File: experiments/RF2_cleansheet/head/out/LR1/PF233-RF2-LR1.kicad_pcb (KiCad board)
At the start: 2 copper layers, 150 x 150 mm, 94 parts

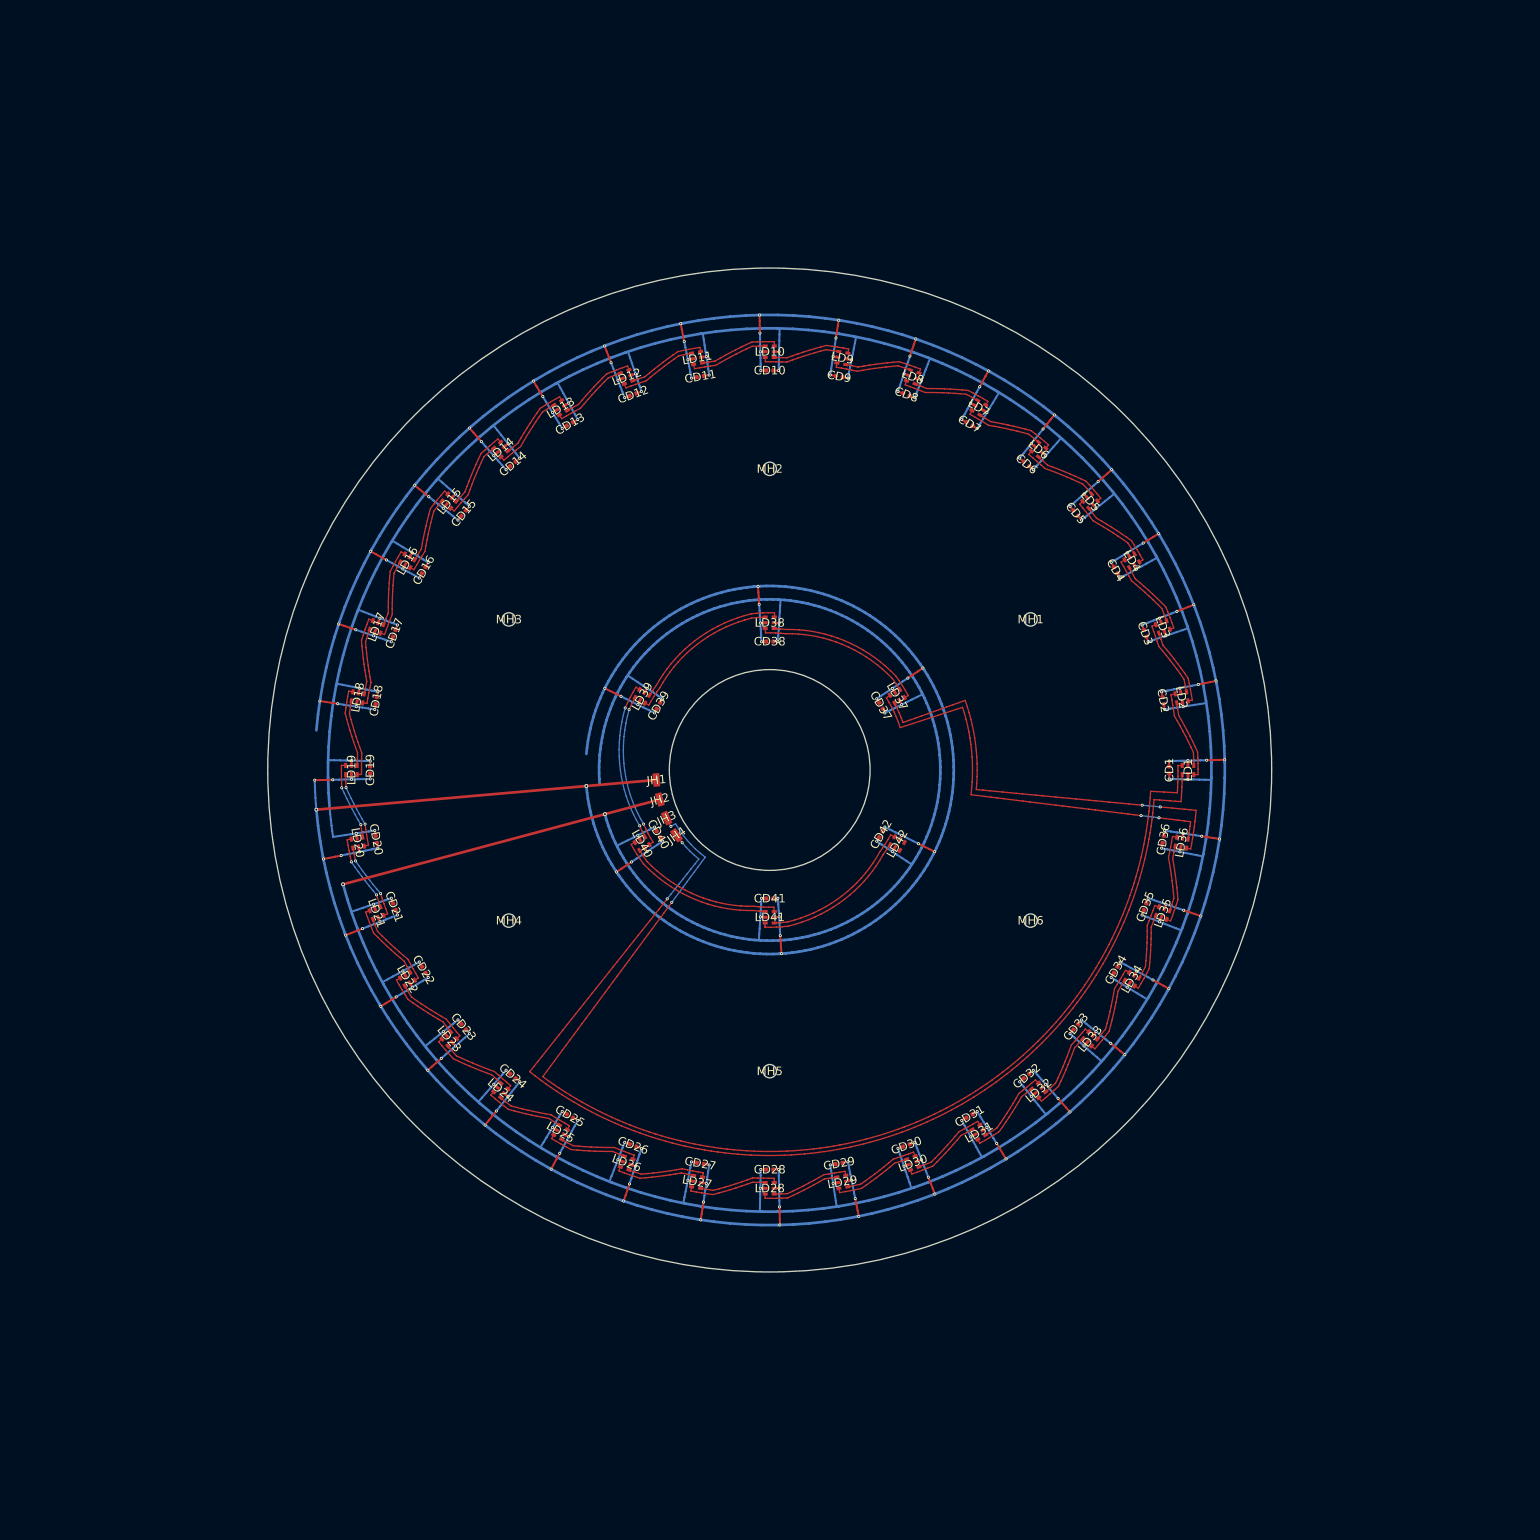
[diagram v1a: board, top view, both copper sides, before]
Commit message: RF2 WIP: dense LED display flex LR1 (522 SK9822-EC20, 13 rings rim to centre), template-routed, KiCad DRC 0 / 0 unconnected
rf2_ledgrid.py is the single source of the display's outline, parts, nets and copper: 12 rings r 104..16 on an 8 mm grid + a 4-LED centre ring,
alternating CCW / CW cells sharing open B.Cu buses, two B.Cu spokes (power tree), 4 serpentine chains (48 / 101 / 158 / 215 LEDs), hinge flap
above CB1D with 12 lands, notch around the gland boss, 6 rim holes. Min clearance 0.15 mm (rule 0.10), no loop around the axis, parity, Gerbers.
Housing, power budget and docs follow.

Co-Authored-By: Claude Opus 5.5 <noreply@anthropic.com>
Claude-Session: https://claude.ai/code/session_01FX4DWSYYjMCFGGA6gmha65
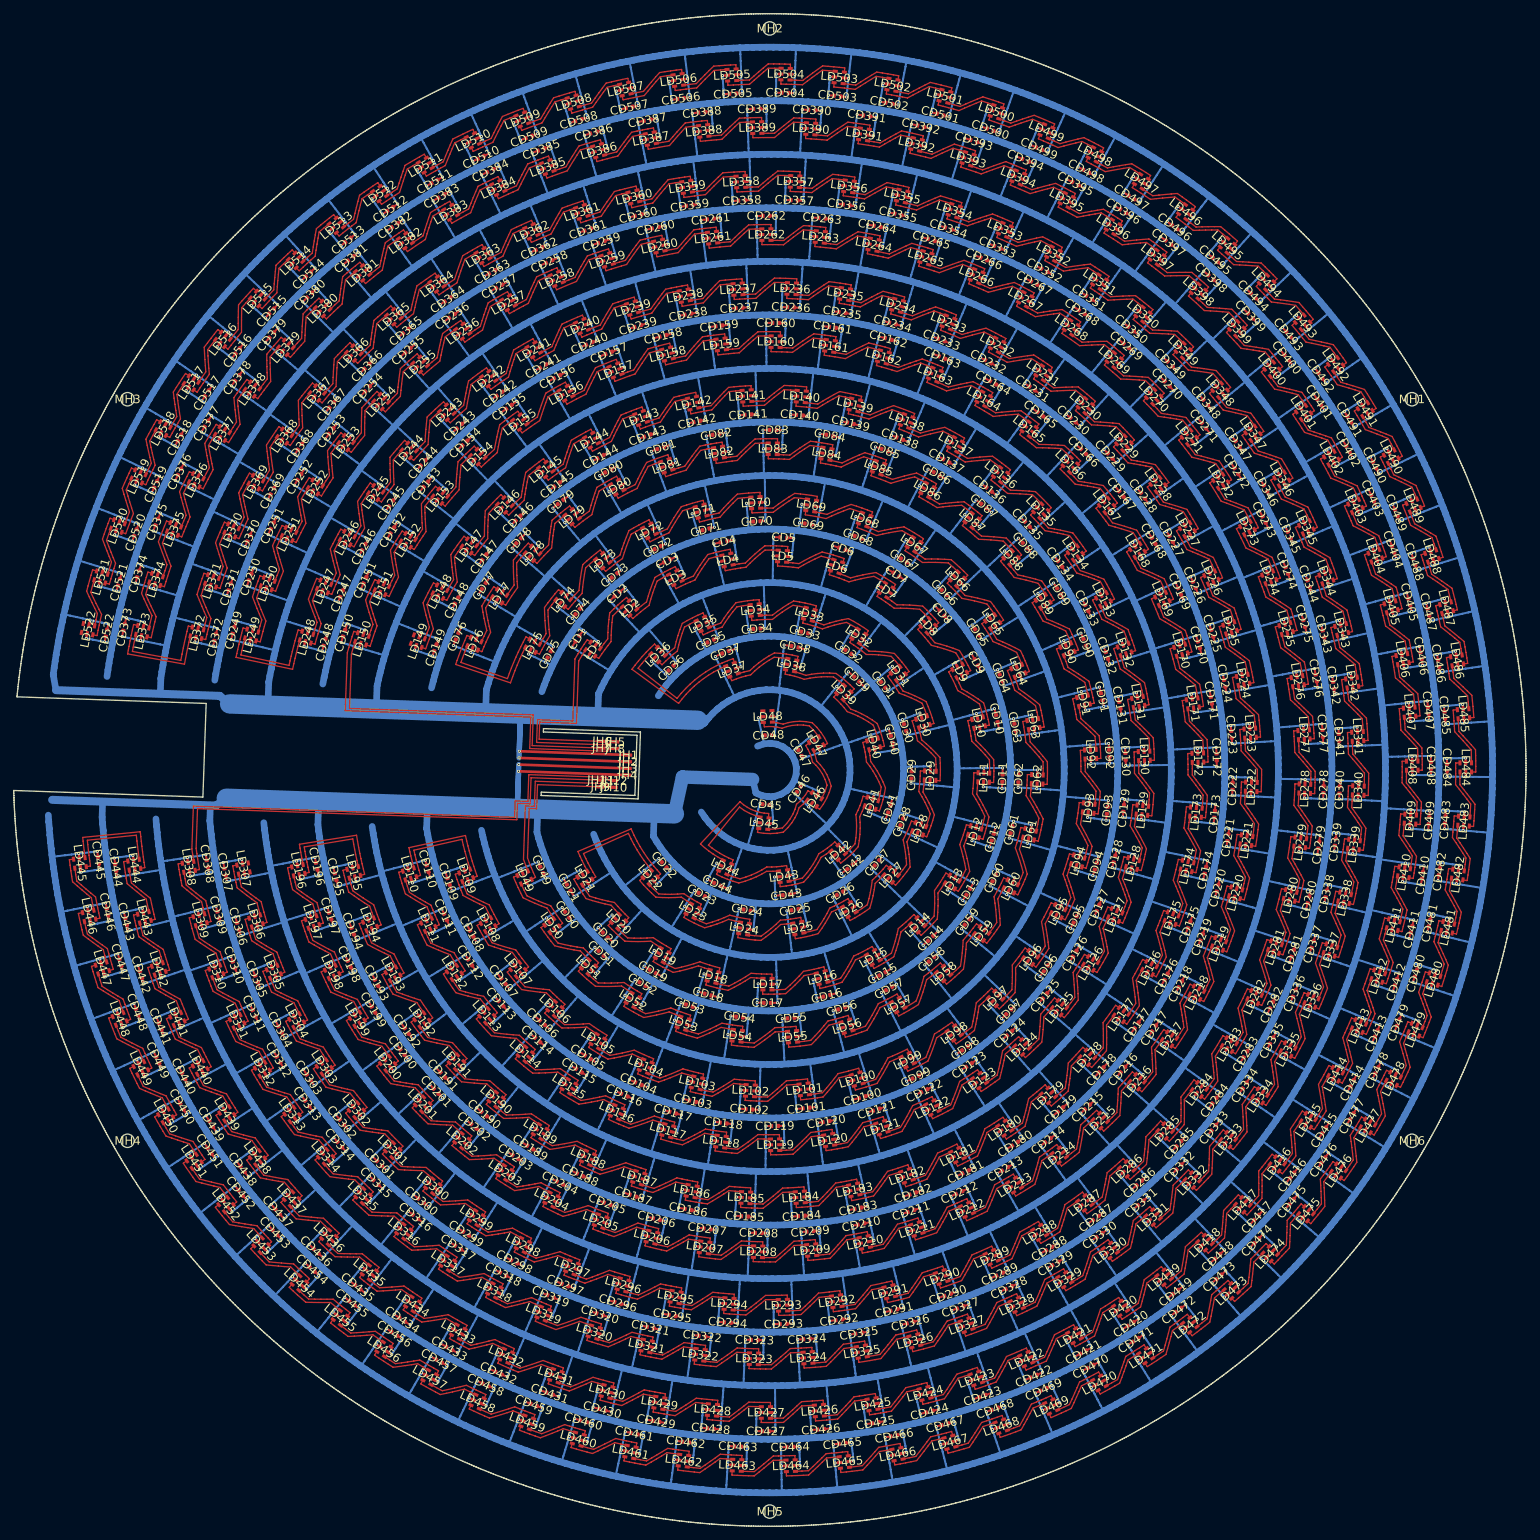
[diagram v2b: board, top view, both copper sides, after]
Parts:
- added CD100: 100n, RF2:C0402, F.Cu at (163.8, 198.9)
- added CD101: 100n, RF2:C0402, F.Cu at (155.5, 200.5)
- added CD102: 100n, RF2:C0402, F.Cu at (146.9, 200.7)
- added CD103: 100n, RF2:C0402, F.Cu at (138.5, 199.5)
- added CD104: 100n, RF2:C0402, F.Cu at (130.4, 196.9)
- added CD105: 100n, RF2:C0402, F.Cu at (122.8, 192.9)
- added CD106: 100n, RF2:C0402, F.Cu at (116.0, 187.8)
- added CD107: 100n, RF2:C0402, F.Cu at (110.2, 181.6)
- added CD108: 100n, RF2:C0402, F.Cu at (105.5, 174.5)
- added CD109: 100n, RF2:C0402, F.Cu at (102.0, 166.7)
- added CD110: 100n, RF2:C0402, F.Cu at (98.9, 164.8)
- added CD111: 100n, RF2:C0402, F.Cu at (101.6, 172.0)
- added CD112: 100n, RF2:C0402, F.Cu at (105.2, 178.7)
- added CD113: 100n, RF2:C0402, F.Cu at (109.9, 184.9)
- added CD114: 100n, RF2:C0402, F.Cu at (115.3, 190.3)
- added CD115: 100n, RF2:C0402, F.Cu at (121.5, 194.9)
- added CD116: 100n, RF2:C0402, F.Cu at (128.3, 198.6)
- added CD117: 100n, RF2:C0402, F.Cu at (135.5, 201.2)
- added CD118: 100n, RF2:C0402, F.Cu at (143.1, 202.7)
- added CD119: 100n, RF2:C0402, F.Cu at (150.8, 203.2)
- added CD120: 100n, RF2:C0402, F.Cu at (158.4, 202.5)
- added CD121: 100n, RF2:C0402, F.Cu at (165.9, 200.8)
- added CD122: 100n, RF2:C0402, F.Cu at (173.1, 197.9)
- added CD123: 100n, RF2:C0402, F.Cu at (179.8, 194.1)
- added CD124: 100n, RF2:C0402, F.Cu at (185.8, 189.3)
- added CD125: 100n, RF2:C0402, F.Cu at (191.1, 183.7)
- added CD126: 100n, RF2:C0402, F.Cu at (195.6, 177.4)
- added CD127: 100n, RF2:C0402, F.Cu at (199.1, 170.6)
- added CD128: 100n, RF2:C0402, F.Cu at (201.5, 163.3)
- added CD129: 100n, RF2:C0402, F.Cu at (202.9, 155.7)
- added CD130: 100n, RF2:C0402, F.Cu at (203.2, 148.0)
- added CD131: 100n, RF2:C0402, F.Cu at (202.3, 140.3)
- added CD132: 100n, RF2:C0402, F.Cu at (200.4, 132.9)
- added CD133: 100n, RF2:C0402, F.Cu at (197.4, 125.8)
- added CD134: 100n, RF2:C0402, F.Cu at (193.4, 119.2)
- added CD135: 100n, RF2:C0402, F.Cu at (188.5, 113.3)
- added CD136: 100n, RF2:C0402, F.Cu at (182.8, 108.1)
- added CD137: 100n, RF2:C0402, F.Cu at (176.4, 103.8)
- added CD138: 100n, RF2:C0402, F.Cu at (169.4, 100.5)
- added CD139: 100n, RF2:C0402, F.Cu at (162.1, 98.2)
- added CD140: 100n, RF2:C0402, F.Cu at (154.5, 97.0)
- added CD141: 100n, RF2:C0402, F.Cu at (146.8, 96.9)
- added CD142: 100n, RF2:C0402, F.Cu at (139.1, 97.9)
- added CD143: 100n, RF2:C0402, F.Cu at (131.7, 100.0)
- added CD144: 100n, RF2:C0402, F.Cu at (124.7, 103.2)
- added CD145: 100n, RF2:C0402, F.Cu at (118.2, 107.3)
- added CD146: 100n, RF2:C0402, F.Cu at (112.4, 112.4)
- added CD147: 100n, RF2:C0402, F.Cu at (107.3, 118.2)
- added CD148: 100n, RF2:C0402, F.Cu at (103.2, 124.7)
- added CD149: 100n, RF2:C0402, F.Cu at (100.0, 131.7)
- added CD150: 100n, RF2:C0402, F.Cu at (86.4, 129.5)
- added CD151: 100n, RF2:C0402, F.Cu at (89.5, 121.6)
- added CD152: 100n, RF2:C0402, F.Cu at (93.6, 114.2)
- added CD153: 100n, RF2:C0402, F.Cu at (98.6, 107.3)
- added CD154: 100n, RF2:C0402, F.Cu at (104.5, 101.1)
- added CD155: 100n, RF2:C0402, F.Cu at (111.0, 95.7)
- added CD156: 100n, RF2:C0402, F.Cu at (118.2, 91.2)
- added CD157: 100n, RF2:C0402, F.Cu at (126.0, 87.7)
- added CD158: 100n, RF2:C0402, F.Cu at (134.1, 85.1)
- added CD159: 100n, RF2:C0402, F.Cu at (142.4, 83.6)
- added CD160: 100n, RF2:C0402, F.Cu at (150.9, 83.2)
- added CD161: 100n, RF2:C0402, F.Cu at (159.4, 83.9)
- added CD162: 100n, RF2:C0402, F.Cu at (167.7, 85.6)
- added CD163: 100n, RF2:C0402, F.Cu at (175.8, 88.4)
- added CD164: 100n, RF2:C0402, F.Cu at (183.4, 92.1)
- added CD165: 100n, RF2:C0402, F.Cu at (190.5, 96.8)
- added CD166: 100n, RF2:C0402, F.Cu at (196.9, 102.4)
- added CD167: 100n, RF2:C0402, F.Cu at (202.5, 108.8)
- added CD168: 100n, RF2:C0402, F.Cu at (207.4, 115.8)
- added CD169: 100n, RF2:C0402, F.Cu at (211.2, 123.3)
- added CD170: 100n, RF2:C0402, F.Cu at (214.1, 131.3)
- added CD171: 100n, RF2:C0402, F.Cu at (216.0, 139.6)
- added CD172: 100n, RF2:C0402, F.Cu at (216.8, 148.1)
- added CD173: 100n, RF2:C0402, F.Cu at (216.5, 156.6)
- added CD174: 100n, RF2:C0402, F.Cu at (215.1, 165.0)
- added CD175: 100n, RF2:C0402, F.Cu at (212.7, 173.1)
- added CD176: 100n, RF2:C0402, F.Cu at (209.2, 180.9)
- added CD177: 100n, RF2:C0402, F.Cu at (204.8, 188.2)
- added CD178: 100n, RF2:C0402, F.Cu at (199.5, 194.8)
- added CD179: 100n, RF2:C0402, F.Cu at (193.4, 200.7)
- added CD180: 100n, RF2:C0402, F.Cu at (186.7, 205.8)
- added CD181: 100n, RF2:C0402, F.Cu at (179.3, 210.0)
- added CD182: 100n, RF2:C0402, F.Cu at (171.4, 213.3)
- added CD183: 100n, RF2:C0402, F.Cu at (163.2, 215.5)
- added CD184: 100n, RF2:C0402, F.Cu at (154.8, 216.6)
- added CD185: 100n, RF2:C0402, F.Cu at (146.3, 216.7)
- added CD186: 100n, RF2:C0402, F.Cu at (137.8, 215.7)
- added CD187: 100n, RF2:C0402, F.Cu at (129.6, 213.6)
- added CD188: 100n, RF2:C0402, F.Cu at (121.7, 210.5)
- added CD189: 100n, RF2:C0402, F.Cu at (114.2, 206.4)
- added CD190: 100n, RF2:C0402, F.Cu at (107.3, 201.4)
- added CD191: 100n, RF2:C0402, F.Cu at (101.2, 195.6)
- added CD192: 100n, RF2:C0402, F.Cu at (95.8, 189.0)
- added CD193: 100n, RF2:C0402, F.Cu at (91.3, 181.8)
- added CD194: 100n, RF2:C0402, F.Cu at (87.7, 174.1)
- added CD195: 100n, RF2:C0402, F.Cu at (85.1, 166.0)
- added CD196: 100n, RF2:C0402, F.Cu at (82.3, 164.4)
- added CD197: 100n, RF2:C0402, F.Cu at (84.3, 171.8)
- added CD198: 100n, RF2:C0402, F.Cu at (87.2, 179.0)
- added CD199: 100n, RF2:C0402, F.Cu at (90.8, 185.8)
- added CD200: 100n, RF2:C0402, F.Cu at (95.1, 192.2)
- added CD201: 100n, RF2:C0402, F.Cu at (100.2, 198.0)
- added CD202: 100n, RF2:C0402, F.Cu at (105.8, 203.2)
- added CD203: 100n, RF2:C0402, F.Cu at (112.0, 207.8)
- added CD204: 100n, RF2:C0402, F.Cu at (118.7, 211.7)
- added CD205: 100n, RF2:C0402, F.Cu at (125.7, 214.8)
- added CD206: 100n, RF2:C0402, F.Cu at (133.1, 217.1)
- added CD207: 100n, RF2:C0402, F.Cu at (140.6, 218.6)
- added CD208: 100n, RF2:C0402, F.Cu at (148.3, 219.2)
- added CD209: 100n, RF2:C0402, F.Cu at (156.0, 218.9)
- added CD210: 100n, RF2:C0402, F.Cu at (163.7, 217.8)
- added CD211: 100n, RF2:C0402, F.Cu at (171.1, 215.9)
- added CD212: 100n, RF2:C0402, F.Cu at (178.3, 213.1)
- added CD213: 100n, RF2:C0402, F.Cu at (185.2, 209.6)
- added CD214: 100n, RF2:C0402, F.Cu at (191.6, 205.3)
- added CD215: 100n, RF2:C0402, F.Cu at (197.5, 200.4)
- added CD216: 100n, RF2:C0402, F.Cu at (202.8, 194.8)
- added CD217: 100n, RF2:C0402, F.Cu at (207.4, 188.6)
- added CD218: 100n, RF2:C0402, F.Cu at (211.4, 182.0)
- added CD219: 100n, RF2:C0402, F.Cu at (214.5, 175.0)
- added CD220: 100n, RF2:C0402, F.Cu at (216.9, 167.6)
- added CD221: 100n, RF2:C0402, F.Cu at (218.5, 160.1)
- added CD222: 100n, RF2:C0402, F.Cu at (219.2, 152.4)
- added CD223: 100n, RF2:C0402, F.Cu at (219.0, 144.7)
- added CD224: 100n, RF2:C0402, F.Cu at (218.0, 137.1)
- added CD225: 100n, RF2:C0402, F.Cu at (216.1, 129.6)
- added CD226: 100n, RF2:C0402, F.Cu at (213.4, 122.4)
- added CD227: 100n, RF2:C0402, F.Cu at (210.0, 115.5)
- added CD228: 100n, RF2:C0402, F.Cu at (205.8, 109.0)
- added CD229: 100n, RF2:C0402, F.Cu at (200.9, 103.1)
- added CD230: 100n, RF2:C0402, F.Cu at (195.3, 97.7)
- added CD231: 100n, RF2:C0402, F.Cu at (189.2, 93.0)
- added CD232: 100n, RF2:C0402, F.Cu at (182.7, 89.0)
- added CD233: 100n, RF2:C0402, F.Cu at (175.7, 85.7)
- added CD234: 100n, RF2:C0402, F.Cu at (168.4, 83.3)
- added CD235: 100n, RF2:C0402, F.Cu at (160.8, 81.7)
- added CD236: 100n, RF2:C0402, F.Cu at (153.2, 80.9)
- added CD237: 100n, RF2:C0402, F.Cu at (145.5, 80.9)
- added CD238: 100n, RF2:C0402, F.Cu at (137.8, 81.9)
- added CD239: 100n, RF2:C0402, F.Cu at (130.3, 83.7)
- added CD240: 100n, RF2:C0402, F.Cu at (123.0, 86.3)
- added CD241: 100n, RF2:C0402, F.Cu at (116.1, 89.7)
- added CD242: 100n, RF2:C0402, F.Cu at (109.6, 93.8)
- added CD243: 100n, RF2:C0402, F.Cu at (103.6, 98.6)
- added CD244: 100n, RF2:C0402, F.Cu at (98.2, 104.1)
- added CD245: 100n, RF2:C0402, F.Cu at (93.4, 110.2)
- added CD246: 100n, RF2:C0402, F.Cu at (89.3, 116.7)
- added CD247: 100n, RF2:C0402, F.Cu at (86.0, 123.6)
- added CD248: 100n, RF2:C0402, F.Cu at (83.5, 130.9)
- added CD249: 100n, RF2:C0402, F.Cu at (69.9, 129.1)
- added CD250: 100n, RF2:C0402, F.Cu at (72.4, 121.2)
- added CD251: 100n, RF2:C0402, F.Cu at (75.7, 113.5)
- added CD252: 100n, RF2:C0402, F.Cu at (79.7, 106.2)
- added CD253: 100n, RF2:C0402, F.Cu at (84.5, 99.4)
- added CD254: 100n, RF2:C0402, F.Cu at (89.9, 93.0)
- added CD255: 100n, RF2:C0402, F.Cu at (95.9, 87.3)
- added CD256: 100n, RF2:C0402, F.Cu at (102.5, 82.2)
- added CD257: 100n, RF2:C0402, F.Cu at (109.6, 77.7)
- added CD258: 100n, RF2:C0402, F.Cu at (117.1, 74.0)
- added CD259: 100n, RF2:C0402, F.Cu at (124.9, 71.1)
- added CD260: 100n, RF2:C0402, F.Cu at (132.9, 69.0)
- added CD261: 100n, RF2:C0402, F.Cu at (141.2, 67.7)
- added CD262: 100n, RF2:C0402, F.Cu at (149.5, 67.2)
- added CD263: 100n, RF2:C0402, F.Cu at (157.8, 67.6)
- added CD264: 100n, RF2:C0402, F.Cu at (166.1, 68.8)
- added CD265: 100n, RF2:C0402, F.Cu at (174.2, 70.8)
- added CD266: 100n, RF2:C0402, F.Cu at (182.0, 73.6)
- added CD267: 100n, RF2:C0402, F.Cu at (189.5, 77.2)
- added CD268: 100n, RF2:C0402, F.Cu at (196.6, 81.6)
- added CD269: 100n, RF2:C0402, F.Cu at (203.3, 86.6)
- added CD270: 100n, RF2:C0402, F.Cu at (209.4, 92.3)
- added CD271: 100n, RF2:C0402, F.Cu at (214.9, 98.6)
- added CD272: 100n, RF2:C0402, F.Cu at (219.7, 105.3)
- added CD273: 100n, RF2:C0402, F.Cu at (223.9, 112.6)
- added CD274: 100n, RF2:C0402, F.Cu at (227.3, 120.2)
- added CD275: 100n, RF2:C0402, F.Cu at (229.9, 128.1)
- added CD276: 100n, RF2:C0402, F.Cu at (231.7, 136.3)
- added CD277: 100n, RF2:C0402, F.Cu at (232.6, 144.6)
- added CD278: 100n, RF2:C0402, F.Cu at (232.7, 152.9)
- added CD279: 100n, RF2:C0402, F.Cu at (232.0, 161.2)
- added CD280: 100n, RF2:C0402, F.Cu at (230.5, 169.4)
- added CD281: 100n, RF2:C0402, F.Cu at (228.1, 177.4)
- added CD282: 100n, RF2:C0402, F.Cu at (225.0, 185.1)
- added CD283: 100n, RF2:C0402, F.Cu at (221.1, 192.5)
- added CD284: 100n, RF2:C0402, F.Cu at (216.4, 199.4)
- added CD285: 100n, RF2:C0402, F.Cu at (211.1, 205.8)
- added CD286: 100n, RF2:C0402, F.Cu at (205.2, 211.7)
- added CD287: 100n, RF2:C0402, F.Cu at (198.7, 216.9)
- added CD288: 100n, RF2:C0402, F.Cu at (191.7, 221.5)
- added CD289: 100n, RF2:C0402, F.Cu at (184.3, 225.3)
- added CD290: 100n, RF2:C0402, F.Cu at (176.6, 228.4)
- added CD291: 100n, RF2:C0402, F.Cu at (168.6, 230.7)
- added CD292: 100n, RF2:C0402, F.Cu at (160.4, 232.1)
- added CD293: 100n, RF2:C0402, F.Cu at (152.0, 232.8)
- added CD294: 100n, RF2:C0402, F.Cu at (143.7, 232.6)
- added CD295: 100n, RF2:C0402, F.Cu at (135.4, 231.5)
- added CD296: 100n, RF2:C0402, F.Cu at (127.3, 229.6)
- added CD297: 100n, RF2:C0402, F.Cu at (119.4, 226.9)
- added CD298: 100n, RF2:C0402, F.Cu at (111.8, 223.5)
- added CD299: 100n, RF2:C0402, F.Cu at (104.6, 219.3)
- added CD300: 100n, RF2:C0402, F.Cu at (97.9, 214.4)
- added CD301: 100n, RF2:C0402, F.Cu at (91.7, 208.8)
- added CD302: 100n, RF2:C0402, F.Cu at (86.1, 202.6)
- added CD303: 100n, RF2:C0402, F.Cu at (81.1, 195.9)
- added CD304: 100n, RF2:C0402, F.Cu at (76.8, 188.8)
- added CD305: 100n, RF2:C0402, F.Cu at (73.3, 181.2)
- added CD306: 100n, RF2:C0402, F.Cu at (70.6, 173.3)
- added CD307: 100n, RF2:C0402, F.Cu at (68.6, 165.2)
- added CD308: 100n, RF2:C0402, F.Cu at (66.0, 164.0)
- added CD309: 100n, RF2:C0402, F.Cu at (67.6, 171.7)
- added CD310: 100n, RF2:C0402, F.Cu at (69.9, 179.1)
- added CD311: 100n, RF2:C0402, F.Cu at (72.9, 186.4)
- added CD312: 100n, RF2:C0402, F.Cu at (76.6, 193.3)
- added CD313: 100n, RF2:C0402, F.Cu at (80.9, 199.8)
- added CD314: 100n, RF2:C0402, F.Cu at (85.8, 206.0)
- added CD315: 100n, RF2:C0402, F.Cu at (91.2, 211.6)
- added CD316: 100n, RF2:C0402, F.Cu at (97.1, 216.8)
- added CD317: 100n, RF2:C0402, F.Cu at (103.4, 221.3)
- added CD318: 100n, RF2:C0402, F.Cu at (110.2, 225.3)
- added CD319: 100n, RF2:C0402, F.Cu at (117.3, 228.7)
- added CD320: 100n, RF2:C0402, F.Cu at (124.6, 231.3)
- added CD321: 100n, RF2:C0402, F.Cu at (132.2, 233.3)
- added CD322: 100n, RF2:C0402, F.Cu at (139.9, 234.6)
- added CD323: 100n, RF2:C0402, F.Cu at (147.7, 235.2)
- added CD324: 100n, RF2:C0402, F.Cu at (155.5, 235.0)
- added CD325: 100n, RF2:C0402, F.Cu at (163.3, 234.2)
- added CD326: 100n, RF2:C0402, F.Cu at (171.0, 232.6)
- added CD327: 100n, RF2:C0402, F.Cu at (178.5, 230.3)
- added CD328: 100n, RF2:C0402, F.Cu at (185.7, 227.3)
- added CD329: 100n, RF2:C0402, F.Cu at (192.7, 223.7)
- added CD330: 100n, RF2:C0402, F.Cu at (199.3, 219.5)
- added CD331: 100n, RF2:C0402, F.Cu at (205.4, 214.7)
- added CD332: 100n, RF2:C0402, F.Cu at (211.1, 209.3)
- added CD333: 100n, RF2:C0402, F.Cu at (216.3, 203.5)
- added CD334: 100n, RF2:C0402, F.Cu at (221.0, 197.1)
- added CD335: 100n, RF2:C0402, F.Cu at (225.0, 190.4)
- added CD336: 100n, RF2:C0402, F.Cu at (228.4, 183.4)
- added CD337: 100n, RF2:C0402, F.Cu at (231.1, 176.0)
- added CD338: 100n, RF2:C0402, F.Cu at (233.2, 168.5)
- added CD339: 100n, RF2:C0402, F.Cu at (234.5, 160.8)
- added CD340: 100n, RF2:C0402, F.Cu at (235.1, 153.0)
- added CD341: 100n, RF2:C0402, F.Cu at (235.1, 145.1)
- added CD342: 100n, RF2:C0402, F.Cu at (234.3, 137.4)
- added CD343: 100n, RF2:C0402, F.Cu at (232.7, 129.7)
- added CD344: 100n, RF2:C0402, F.Cu at (230.5, 122.2)
- added CD345: 100n, RF2:C0402, F.Cu at (227.6, 114.9)
- added CD346: 100n, RF2:C0402, F.Cu at (224.1, 107.9)
- added CD347: 100n, RF2:C0402, F.Cu at (219.9, 101.3)
- added CD348: 100n, RF2:C0402, F.Cu at (215.1, 95.1)
- added CD349: 100n, RF2:C0402, F.Cu at (209.8, 89.3)
- added CD350: 100n, RF2:C0402, F.Cu at (204.0, 84.1)
- added CD351: 100n, RF2:C0402, F.Cu at (197.7, 79.4)
- added CD352: 100n, RF2:C0402, F.Cu at (191.0, 75.3)
- added CD353: 100n, RF2:C0402, F.Cu at (184.0, 71.9)
- added CD354: 100n, RF2:C0402, F.Cu at (176.7, 69.1)
- added CD355: 100n, RF2:C0402, F.Cu at (169.2, 67.0)
- added CD356: 100n, RF2:C0402, F.Cu at (161.5, 65.6)
- added CD357: 100n, RF2:C0402, F.Cu at (153.7, 64.9)
- added CD358: 100n, RF2:C0402, F.Cu at (145.8, 64.9)
- added CD359: 100n, RF2:C0402, F.Cu at (138.0, 65.6)
- added CD360: 100n, RF2:C0402, F.Cu at (130.3, 67.1)
- added CD361: 100n, RF2:C0402, F.Cu at (122.8, 69.3)
- added CD362: 100n, RF2:C0402, F.Cu at (115.5, 72.1)
- added CD363: 100n, RF2:C0402, F.Cu at (108.5, 75.6)
- added CD364: 100n, RF2:C0402, F.Cu at (101.9, 79.7)
- added CD365: 100n, RF2:C0402, F.Cu at (95.6, 84.4)
- added CD366: 100n, RF2:C0402, F.Cu at (89.8, 89.7)
- added CD367: 100n, RF2:C0402, F.Cu at (84.5, 95.5)
- added CD368: 100n, RF2:C0402, F.Cu at (79.8, 101.7)
- added CD369: 100n, RF2:C0402, F.Cu at (75.7, 108.4)
- added CD370: 100n, RF2:C0402, F.Cu at (72.2, 115.4)
- added CD371: 100n, RF2:C0402, F.Cu at (69.3, 122.6)
- added CD372: 100n, RF2:C0402, F.Cu at (67.1, 130.2)
- added CD373: 100n, RF2:C0402, F.Cu at (53.5, 128.7)
- added CD374: 100n, RF2:C0402, F.Cu at (55.6, 120.7)
- added CD375: 100n, RF2:C0402, F.Cu at (58.4, 112.9)
- added CD376: 100n, RF2:C0402, F.Cu at (61.8, 105.4)
- added CD377: 100n, RF2:C0402, F.Cu at (65.8, 98.3)
- added CD378: 100n, RF2:C0402, F.Cu at (70.4, 91.4)
- added CD379: 100n, RF2:C0402, F.Cu at (75.6, 85.0)
- added CD380: 100n, RF2:C0402, F.Cu at (81.2, 79.0)
- added CD381: 100n, RF2:C0402, F.Cu at (87.4, 73.6)
- added CD382: 100n, RF2:C0402, F.Cu at (94.0, 68.6)
- added CD383: 100n, RF2:C0402, F.Cu at (100.9, 64.2)
- added CD384: 100n, RF2:C0402, F.Cu at (108.3, 60.5)
- added CD385: 100n, RF2:C0402, F.Cu at (115.9, 57.3)
- added CD386: 100n, RF2:C0402, F.Cu at (123.7, 54.8)
- added CD387: 100n, RF2:C0402, F.Cu at (131.7, 52.9)
- added CD388: 100n, RF2:C0402, F.Cu at (139.9, 51.7)
- added CD389: 100n, RF2:C0402, F.Cu at (148.1, 51.2)
- added CD390: 100n, RF2:C0402, F.Cu at (156.3, 51.4)
- added CD391: 100n, RF2:C0402, F.Cu at (164.5, 52.3)
- added CD392: 100n, RF2:C0402, F.Cu at (172.6, 53.8)
- added CD393: 100n, RF2:C0402, F.Cu at (180.5, 56.0)
- added CD394: 100n, RF2:C0402, F.Cu at (188.2, 58.9)
- added CD395: 100n, RF2:C0402, F.Cu at (195.7, 62.4)
- added CD396: 100n, RF2:C0402, F.Cu at (202.8, 66.5)
- added CD397: 100n, RF2:C0402, F.Cu at (209.6, 71.2)
- added CD398: 100n, RF2:C0402, F.Cu at (215.9, 76.4)
- added CD399: 100n, RF2:C0402, F.Cu at (221.8, 82.2)
- added CD400: 100n, RF2:C0402, F.Cu at (227.2, 88.4)
- added CD401: 100n, RF2:C0402, F.Cu at (232.1, 95.0)
- added CD402: 100n, RF2:C0402, F.Cu at (236.4, 102.0)
- added CD403: 100n, RF2:C0402, F.Cu at (240.1, 109.4)
- added CD404: 100n, RF2:C0402, F.Cu at (243.1, 117.0)
- added CD405: 100n, RF2:C0402, F.Cu at (245.6, 124.9)
- added CD406: 100n, RF2:C0402, F.Cu at (247.3, 132.9)
- added CD407: 100n, RF2:C0402, F.Cu at (248.4, 141.1)
- added CD408: 100n, RF2:C0402, F.Cu at (248.8, 149.3)
- added CD409: 100n, RF2:C0402, F.Cu at (248.5, 157.6)
- added CD410: 100n, RF2:C0402, F.Cu at (247.5, 165.7)
- added CD411: 100n, RF2:C0402, F.Cu at (245.9, 173.8)
- added CD412: 100n, RF2:C0402, F.Cu at (243.6, 181.7)
- added CD413: 100n, RF2:C0402, F.Cu at (240.6, 189.4)
- added CD414: 100n, RF2:C0402, F.Cu at (237.0, 196.8)
- added CD415: 100n, RF2:C0402, F.Cu at (232.8, 203.9)
- added CD416: 100n, RF2:C0402, F.Cu at (228.1, 210.6)
- added CD417: 100n, RF2:C0402, F.Cu at (222.7, 216.9)
- added CD418: 100n, RF2:C0402, F.Cu at (216.9, 222.7)
- added CD419: 100n, RF2:C0402, F.Cu at (210.6, 228.0)
- added CD420: 100n, RF2:C0402, F.Cu at (203.9, 232.8)
- added CD421: 100n, RF2:C0402, F.Cu at (196.9, 237.0)
- added CD422: 100n, RF2:C0402, F.Cu at (189.4, 240.6)
- added CD423: 100n, RF2:C0402, F.Cu at (181.8, 243.6)
- added CD424: 100n, RF2:C0402, F.Cu at (173.9, 245.9)
- added CD425: 100n, RF2:C0402, F.Cu at (165.8, 247.5)
- added CD426: 100n, RF2:C0402, F.Cu at (157.6, 248.5)
- added CD427: 100n, RF2:C0402, F.Cu at (149.4, 248.8)
- added CD428: 100n, RF2:C0402, F.Cu at (141.2, 248.4)
- added CD429: 100n, RF2:C0402, F.Cu at (133.0, 247.3)
- added CD43: 100n, RF2:C0402, F.Cu at (152.5, 168.6)
- added CD430: 100n, RF2:C0402, F.Cu at (125.0, 245.6)
- added CD431: 100n, RF2:C0402, F.Cu at (117.1, 243.2)
- added CD432: 100n, RF2:C0402, F.Cu at (109.5, 240.1)
- added CD433: 100n, RF2:C0402, F.Cu at (102.1, 236.4)
- added CD434: 100n, RF2:C0402, F.Cu at (95.1, 232.1)
- added CD435: 100n, RF2:C0402, F.Cu at (88.4, 227.3)
- added CD436: 100n, RF2:C0402, F.Cu at (82.2, 221.9)
- added CD437: 100n, RF2:C0402, F.Cu at (76.5, 216.0)
- added CD438: 100n, RF2:C0402, F.Cu at (71.2, 209.6)
- added CD439: 100n, RF2:C0402, F.Cu at (66.5, 202.9)
- added CD44: 100n, RF2:C0402, F.Cu at (142.2, 167.1)
- added CD440: 100n, RF2:C0402, F.Cu at (62.4, 195.7)
- added CD441: 100n, RF2:C0402, F.Cu at (58.9, 188.3)
- added CD442: 100n, RF2:C0402, F.Cu at (56.1, 180.6)
- added CD443: 100n, RF2:C0402, F.Cu at (53.8, 172.6)
- added CD444: 100n, RF2:C0402, F.Cu at (52.3, 164.6)
- added CD445: 100n, RF2:C0402, F.Cu at (49.7, 163.5)
- added CD446: 100n, RF2:C0402, F.Cu at (51.0, 171.2)
- added CD447: 100n, RF2:C0402, F.Cu at (53.0, 178.8)
- added CD448: 100n, RF2:C0402, F.Cu at (55.5, 186.2)
- added CD449: 100n, RF2:C0402, F.Cu at (58.6, 193.4)
- added CD45: 100n, RF2:C0402, F.Cu at (149.4, 155.2)
- added CD450: 100n, RF2:C0402, F.Cu at (62.2, 200.3)
- added CD451: 100n, RF2:C0402, F.Cu at (66.3, 206.9)
- added CD452: 100n, RF2:C0402, F.Cu at (71.0, 213.2)
- added CD453: 100n, RF2:C0402, F.Cu at (76.1, 219.1)
- added CD454: 100n, RF2:C0402, F.Cu at (81.6, 224.6)
- added CD455: 100n, RF2:C0402, F.Cu at (87.6, 229.7)
- added CD456: 100n, RF2:C0402, F.Cu at (93.9, 234.2)
- added CD457: 100n, RF2:C0402, F.Cu at (100.6, 238.3)
- added CD458: 100n, RF2:C0402, F.Cu at (107.5, 241.9)
- added CD459: 100n, RF2:C0402, F.Cu at (114.7, 244.9)
- added CD46: 100n, RF2:C0402, F.Cu at (154.3, 152.9)
- added CD460: 100n, RF2:C0402, F.Cu at (122.2, 247.3)
- added CD461: 100n, RF2:C0402, F.Cu at (129.8, 249.2)
- added CD462: 100n, RF2:C0402, F.Cu at (137.5, 250.4)
- added CD463: 100n, RF2:C0402, F.Cu at (145.2, 251.1)
- added CD464: 100n, RF2:C0402, F.Cu at (153.1, 251.2)
- added CD465: 100n, RF2:C0402, F.Cu at (160.8, 250.6)
- added CD466: 100n, RF2:C0402, F.Cu at (168.6, 249.5)
- added CD467: 100n, RF2:C0402, F.Cu at (176.2, 247.8)
- added CD468: 100n, RF2:C0402, F.Cu at (183.7, 245.4)
- added CD469: 100n, RF2:C0402, F.Cu at (190.9, 242.6)
- added CD47: 100n, RF2:C0402, F.Cu at (154.5, 147.4)
- added CD470: 100n, RF2:C0402, F.Cu at (197.9, 239.1)
- added CD471: 100n, RF2:C0402, F.Cu at (204.7, 235.2)
- added CD472: 100n, RF2:C0402, F.Cu at (211.1, 230.7)
- added CD473: 100n, RF2:C0402, F.Cu at (217.1, 225.7)
- added CD474: 100n, RF2:C0402, F.Cu at (222.8, 220.3)
- added CD475: 100n, RF2:C0402, F.Cu at (228.0, 214.5)
- added CD476: 100n, RF2:C0402, F.Cu at (232.7, 208.3)
- added CD477: 100n, RF2:C0402, F.Cu at (237.0, 201.8)
- added CD478: 100n, RF2:C0402, F.Cu at (240.7, 194.9)
- added CD479: 100n, RF2:C0402, F.Cu at (243.9, 187.8)
- added CD48: 100n, RF2:C0402, F.Cu at (149.8, 144.8)
- added CD480: 100n, RF2:C0402, F.Cu at (246.5, 180.4)
- added CD481: 100n, RF2:C0402, F.Cu at (248.6, 172.9)
- added CD482: 100n, RF2:C0402, F.Cu at (250.1, 165.2)
- added CD483: 100n, RF2:C0402, F.Cu at (250.9, 157.4)
- added CD484: 100n, RF2:C0402, F.Cu at (251.2, 149.6)
- added CD485: 100n, RF2:C0402, F.Cu at (250.9, 141.8)
- added CD486: 100n, RF2:C0402, F.Cu at (249.9, 134.1)
- added CD487: 100n, RF2:C0402, F.Cu at (248.4, 126.4)
- added CD488: 100n, RF2:C0402, F.Cu at (246.3, 118.9)
- added CD489: 100n, RF2:C0402, F.Cu at (243.6, 111.5)
- added CD49: 100n, RF2:C0402, F.Cu at (115.9, 164.9)
- added CD490: 100n, RF2:C0402, F.Cu at (240.4, 104.4)
- added CD491: 100n, RF2:C0402, F.Cu at (236.6, 97.6)
- added CD492: 100n, RF2:C0402, F.Cu at (232.3, 91.1)
- added CD493: 100n, RF2:C0402, F.Cu at (227.5, 84.9)
- added CD494: 100n, RF2:C0402, F.Cu at (222.2, 79.1)
- added CD495: 100n, RF2:C0402, F.Cu at (216.6, 73.8)
- added CD496: 100n, RF2:C0402, F.Cu at (210.5, 68.9)
- added CD497: 100n, RF2:C0402, F.Cu at (204.0, 64.4)
- added CD498: 100n, RF2:C0402, F.Cu at (197.3, 60.5)
- added CD499: 100n, RF2:C0402, F.Cu at (190.2, 57.1)
- added CD50: 100n, RF2:C0402, F.Cu at (119.7, 171.6)
- added CD500: 100n, RF2:C0402, F.Cu at (183.0, 54.3)
- added CD501: 100n, RF2:C0402, F.Cu at (175.5, 52.1)
- added CD502: 100n, RF2:C0402, F.Cu at (167.8, 50.4)
- added CD503: 100n, RF2:C0402, F.Cu at (160.1, 49.3)
- added CD504: 100n, RF2:C0402, F.Cu at (152.3, 48.8)
- added CD505: 100n, RF2:C0402, F.Cu at (144.5, 48.9)
- added CD506: 100n, RF2:C0402, F.Cu at (136.7, 49.7)
- added CD507: 100n, RF2:C0402, F.Cu at (129.0, 51.0)
- added CD508: 100n, RF2:C0402, F.Cu at (121.4, 52.9)
- added CD509: 100n, RF2:C0402, F.Cu at (114.0, 55.4)
- added CD51: 100n, RF2:C0402, F.Cu at (124.8, 177.4)
- added CD510: 100n, RF2:C0402, F.Cu at (106.8, 58.5)
- added CD511: 100n, RF2:C0402, F.Cu at (99.9, 62.1)
- added CD512: 100n, RF2:C0402, F.Cu at (93.3, 66.2)
- added CD513: 100n, RF2:C0402, F.Cu at (87.0, 70.8)
- added CD514: 100n, RF2:C0402, F.Cu at (81.1, 75.9)
- added CD515: 100n, RF2:C0402, F.Cu at (75.6, 81.4)
- added CD516: 100n, RF2:C0402, F.Cu at (70.5, 87.4)
- added CD517: 100n, RF2:C0402, F.Cu at (65.9, 93.7)
- added CD518: 100n, RF2:C0402, F.Cu at (61.8, 100.4)
- added CD519: 100n, RF2:C0402, F.Cu at (58.2, 107.3)
- added CD52: 100n, RF2:C0402, F.Cu at (131.0, 182.0)
- added CD520: 100n, RF2:C0402, F.Cu at (55.2, 114.5)
- added CD521: 100n, RF2:C0402, F.Cu at (52.8, 121.9)
- added CD522: 100n, RF2:C0402, F.Cu at (50.9, 129.5)
- added CD53: 100n, RF2:C0402, F.Cu at (138.0, 185.2)
- added CD54: 100n, RF2:C0402, F.Cu at (145.5, 186.9)
- added CD55: 100n, RF2:C0402, F.Cu at (153.2, 187.1)
- added CD56: 100n, RF2:C0402, F.Cu at (160.7, 185.6)
- added CD57: 100n, RF2:C0402, F.Cu at (167.8, 182.6)
- added CD58: 100n, RF2:C0402, F.Cu at (174.2, 178.3)
- added CD59: 100n, RF2:C0402, F.Cu at (179.5, 172.7)
- added CD60: 100n, RF2:C0402, F.Cu at (183.5, 166.2)
- added CD61: 100n, RF2:C0402, F.Cu at (186.1, 158.9)
- added CD62: 100n, RF2:C0402, F.Cu at (187.2, 151.3)
- added CD63: 100n, RF2:C0402, F.Cu at (186.6, 143.6)
- added CD64: 100n, RF2:C0402, F.Cu at (184.6, 136.2)
- added CD65: 100n, RF2:C0402, F.Cu at (181.0, 129.4)
- added CD66: 100n, RF2:C0402, F.Cu at (176.1, 123.5)
- added CD67: 100n, RF2:C0402, F.Cu at (170.1, 118.7)
- added CD68: 100n, RF2:C0402, F.Cu at (163.2, 115.2)
- added CD69: 100n, RF2:C0402, F.Cu at (155.8, 113.2)
- added CD70: 100n, RF2:C0402, F.Cu at (148.1, 112.9)
- added CD71: 100n, RF2:C0402, F.Cu at (140.5, 114.0)
- added CD72: 100n, RF2:C0402, F.Cu at (133.3, 116.8)
- added CD73: 100n, RF2:C0402, F.Cu at (126.8, 120.9)
- added CD74: 100n, RF2:C0402, F.Cu at (121.3, 126.3)
- added CD75: 100n, RF2:C0402, F.Cu at (117.1, 132.7)
- added CD76: 100n, RF2:C0402, F.Cu at (103.3, 130.0)
- added CD77: 100n, RF2:C0402, F.Cu at (107.3, 122.5)
- added CD78: 100n, RF2:C0402, F.Cu at (112.5, 115.7)
- added CD79: 100n, RF2:C0402, F.Cu at (118.7, 110.0)
- added CD80: 100n, RF2:C0402, F.Cu at (125.9, 105.3)
- added CD81: 100n, RF2:C0402, F.Cu at (133.7, 101.9)
- added CD82: 100n, RF2:C0402, F.Cu at (142.0, 99.8)
- added CD83: 100n, RF2:C0402, F.Cu at (150.5, 99.2)
- added CD84: 100n, RF2:C0402, F.Cu at (159.0, 100.0)
- added CD85: 100n, RF2:C0402, F.Cu at (167.2, 102.2)
- added CD86: 100n, RF2:C0402, F.Cu at (175.0, 105.8)
- added CD87: 100n, RF2:C0402, F.Cu at (182.0, 110.5)
- added CD88: 100n, RF2:C0402, F.Cu at (188.2, 116.5)
- added CD89: 100n, RF2:C0402, F.Cu at (193.2, 123.3)
- added CD90: 100n, RF2:C0402, F.Cu at (197.1, 130.9)
- added CD91: 100n, RF2:C0402, F.Cu at (199.6, 139.1)
- added CD92: 100n, RF2:C0402, F.Cu at (200.7, 147.5)
- added CD93: 100n, RF2:C0402, F.Cu at (200.4, 156.0)
- added CD94: 100n, RF2:C0402, F.Cu at (198.7, 164.4)
- added CD95: 100n, RF2:C0402, F.Cu at (195.6, 172.3)
- added CD96: 100n, RF2:C0402, F.Cu at (191.3, 179.6)
- added CD97: 100n, RF2:C0402, F.Cu at (185.7, 186.1)
- added CD98: 100n, RF2:C0402, F.Cu at (179.2, 191.6)
- added CD99: 100n, RF2:C0402, F.Cu at (171.8, 195.9)
- added JH10: C2_D0, RF2:FLEX_LAND, F.Cu at (126.7, 152.6)
- added JH11: C4_K0, RF2:FLEX_LAND, F.Cu at (124.7, 151.5)
- added JH12: C4_D0, RF2:FLEX_LAND, F.Cu at (126.7, 151.6)
- added JH5: C1_K0, RF2:FLEX_LAND, F.Cu at (126.9, 145.8)
- added JH6: C1_D0, RF2:FLEX_LAND, F.Cu at (124.9, 145.7)
- added JH7: C3_D0, RF2:FLEX_LAND, F.Cu at (124.9, 146.7)
- added JH8: C3_K0, RF2:FLEX_LAND, F.Cu at (126.9, 146.8)
- added JH9: C2_K0, RF2:FLEX_LAND, F.Cu at (124.7, 152.5)
- added LD100: SK9822-EC20, RF2:SK9822EC20, F.Cu at (163.1, 196.2)
- added LD101: SK9822-EC20, RF2:SK9822EC20, F.Cu at (155.2, 197.7)
- added LD102: SK9822-EC20, RF2:SK9822EC20, F.Cu at (147.1, 197.9)
- added LD103: SK9822-EC20, RF2:SK9822EC20, F.Cu at (139.1, 196.8)
- added LD104: SK9822-EC20, RF2:SK9822EC20, F.Cu at (131.5, 194.3)
- added LD105: SK9822-EC20, RF2:SK9822EC20, F.Cu at (124.3, 190.6)
- added LD106: SK9822-EC20, RF2:SK9822EC20, F.Cu at (117.9, 185.7)
- added LD107: SK9822-EC20, RF2:SK9822EC20, F.Cu at (112.4, 179.8)
- added LD108: SK9822-EC20, RF2:SK9822EC20, F.Cu at (107.9, 173.1)
- added LD109: SK9822-EC20, RF2:SK9822EC20, F.Cu at (104.7, 165.7)
- added LD110: SK9822-EC20, RF2:SK9822EC20, F.Cu at (96.2, 165.5)
- added LD111: SK9822-EC20, RF2:SK9822EC20, F.Cu at (99.0, 173.1)
- added LD112: SK9822-EC20, RF2:SK9822EC20, F.Cu at (102.9, 180.3)
- added LD113: SK9822-EC20, RF2:SK9822EC20, F.Cu at (107.7, 186.7)
- added LD114: SK9822-EC20, RF2:SK9822EC20, F.Cu at (113.5, 192.5)
- added LD115: SK9822-EC20, RF2:SK9822EC20, F.Cu at (120.0, 197.3)
- added LD116: SK9822-EC20, RF2:SK9822EC20, F.Cu at (127.1, 201.1)
- added LD117: SK9822-EC20, RF2:SK9822EC20, F.Cu at (134.8, 203.9)
- added LD118: SK9822-EC20, RF2:SK9822EC20, F.Cu at (142.7, 205.5)
- added LD119: SK9822-EC20, RF2:SK9822EC20, F.Cu at (150.8, 206.0)
- added LD120: SK9822-EC20, RF2:SK9822EC20, F.Cu at (158.9, 205.3)
- added LD121: SK9822-EC20, RF2:SK9822EC20, F.Cu at (166.8, 203.4)
- added LD122: SK9822-EC20, RF2:SK9822EC20, F.Cu at (174.3, 200.4)
- added LD123: SK9822-EC20, RF2:SK9822EC20, F.Cu at (181.3, 196.4)
- added LD124: SK9822-EC20, RF2:SK9822EC20, F.Cu at (187.7, 191.4)
- added LD125: SK9822-EC20, RF2:SK9822EC20, F.Cu at (193.3, 185.5)
- added LD126: SK9822-EC20, RF2:SK9822EC20, F.Cu at (198.0, 178.9)
- added LD127: SK9822-EC20, RF2:SK9822EC20, F.Cu at (201.6, 171.7)
- added LD128: SK9822-EC20, RF2:SK9822EC20, F.Cu at (204.2, 164.0)
- added LD129: SK9822-EC20, RF2:SK9822EC20, F.Cu at (205.7, 156.0)
- added LD130: SK9822-EC20, RF2:SK9822EC20, F.Cu at (206.0, 147.9)
- added LD131: SK9822-EC20, RF2:SK9822EC20, F.Cu at (205.1, 139.8)
- added LD132: SK9822-EC20, RF2:SK9822EC20, F.Cu at (203.0, 132.0)
- added LD133: SK9822-EC20, RF2:SK9822EC20, F.Cu at (199.9, 124.5)
- added LD134: SK9822-EC20, RF2:SK9822EC20, F.Cu at (195.7, 117.6)
- added LD135: SK9822-EC20, RF2:SK9822EC20, F.Cu at (190.5, 111.3)
- added LD136: SK9822-EC20, RF2:SK9822EC20, F.Cu at (184.5, 105.9)
- added LD137: SK9822-EC20, RF2:SK9822EC20, F.Cu at (177.8, 101.4)
- added LD138: SK9822-EC20, RF2:SK9822EC20, F.Cu at (170.5, 97.9)
- added LD139: SK9822-EC20, RF2:SK9822EC20, F.Cu at (162.7, 95.5)
- added LD140: SK9822-EC20, RF2:SK9822EC20, F.Cu at (154.7, 94.2)
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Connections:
- net LED_C1 renamed C1_K1
- net LED_C10 renamed C1_K10
- net LED_C11 renamed C1_K11
- net LED_C12 renamed C1_K12
- net LED_C13 renamed C1_K13
- net LED_C14 renamed C1_K14
- net LED_C15 renamed C1_K15
- net LED_C16 renamed C1_K16
- net LED_C17 renamed C1_K17
- net LED_C18 renamed C1_K18
- net LED_C19 renamed C1_K19
- net LED_C2 renamed C1_K2
- net LED_C20 renamed C1_K20
- net LED_C21 renamed C1_K21
- net LED_C22 renamed C1_K22
- net LED_C23 renamed C1_K23
- net LED_C24 renamed C1_K24
- net LED_C25 renamed C1_K25
- net LED_C26 renamed C1_K26
- net LED_C27 renamed C1_K27
- net LED_C28 renamed C1_K28
- net LED_C29 renamed C1_K29
- net LED_C3 renamed C1_K3
- net LED_C30 renamed C1_K30
- net LED_C31 renamed C1_K31
- net LED_C32 renamed C1_K32
- net LED_C33 renamed C1_K33
- net LED_C34 renamed C1_K34
- net LED_C35 renamed C1_K35
- net LED_C36 renamed C1_K36
- net LED_C37 renamed C1_K37
- net LED_C38 renamed C1_K38
- net LED_C39 renamed C1_K39
- net LED_C4 renamed C1_K4
- net LED_C40 renamed C1_K40
- net LED_C41 renamed C1_K41
- net LED_C5 renamed C1_K5
- net LED_C6 renamed C1_K6
- net LED_C7 renamed C1_K7
- net LED_C8 renamed C1_K8
- net LED_C9 renamed C1_K9
- net LED_D1 renamed C1_D1
- net LED_D10 renamed C1_D10
- net LED_D11 renamed C1_D11
- net LED_D12 renamed C1_D12
- net LED_D13 renamed C1_D13
- net LED_D14 renamed C1_D14
- net LED_D15 renamed C1_D15
- net LED_D16 renamed C1_D16
- net LED_D17 renamed C1_D17
- net LED_D18 renamed C1_D18
- net LED_D19 renamed C1_D19
- net LED_D2 renamed C1_D2
- net LED_D20 renamed C1_D20
- net LED_D21 renamed C1_D21
- net LED_D22 renamed C1_D22
- net LED_D23 renamed C1_D23
- net LED_D24 renamed C1_D24
- net LED_D25 renamed C1_D25
- net LED_D26 renamed C1_D26
- net LED_D27 renamed C1_D27
- net LED_D28 renamed C1_D28
- net LED_D29 renamed C1_D29
- net LED_D3 renamed C1_D3
- net LED_D30 renamed C1_D30
- net LED_D31 renamed C1_D31
- net LED_D32 renamed C1_D32
- net LED_D33 renamed C1_D33
- net LED_D34 renamed C1_D34
- net LED_D35 renamed C1_D35
- net LED_D36 renamed C1_D36
- net LED_D37 renamed C1_D37
- net LED_D38 renamed C1_D38
- net LED_D39 renamed C1_D39
- net LED_D4 renamed C1_D4
- net LED_D40 renamed C1_D40
- net LED_D41 renamed C1_D41
- net LED_D5 renamed C1_D5
- net LED_D6 renamed C1_D6
- net LED_D7 renamed C1_D7
- net LED_D8 renamed C1_D8
- net LED_D9 renamed C1_D9
- JH1 pad 1: +5V_LED -> GND
- JH3 pad 1: LED_C0 -> +5V_LED
- JH4 pad 1: LED_D0 -> +5V_LED
- LD1 pad 3: LED_D0 -> C1_D0
- LD1 pad 4: LED_C0 -> C1_K0
- LD42 pad 1: LED_DEND -> C1_D42
- LD42 pad 6: LED_CEND -> C1_K42
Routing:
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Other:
- board size 150 x 150 mm -> 226 x 226 mm
